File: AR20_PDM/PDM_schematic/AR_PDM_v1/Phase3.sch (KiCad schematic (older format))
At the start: 15 parts, among them Q1 BTS50025-1TAD, U1 INA233

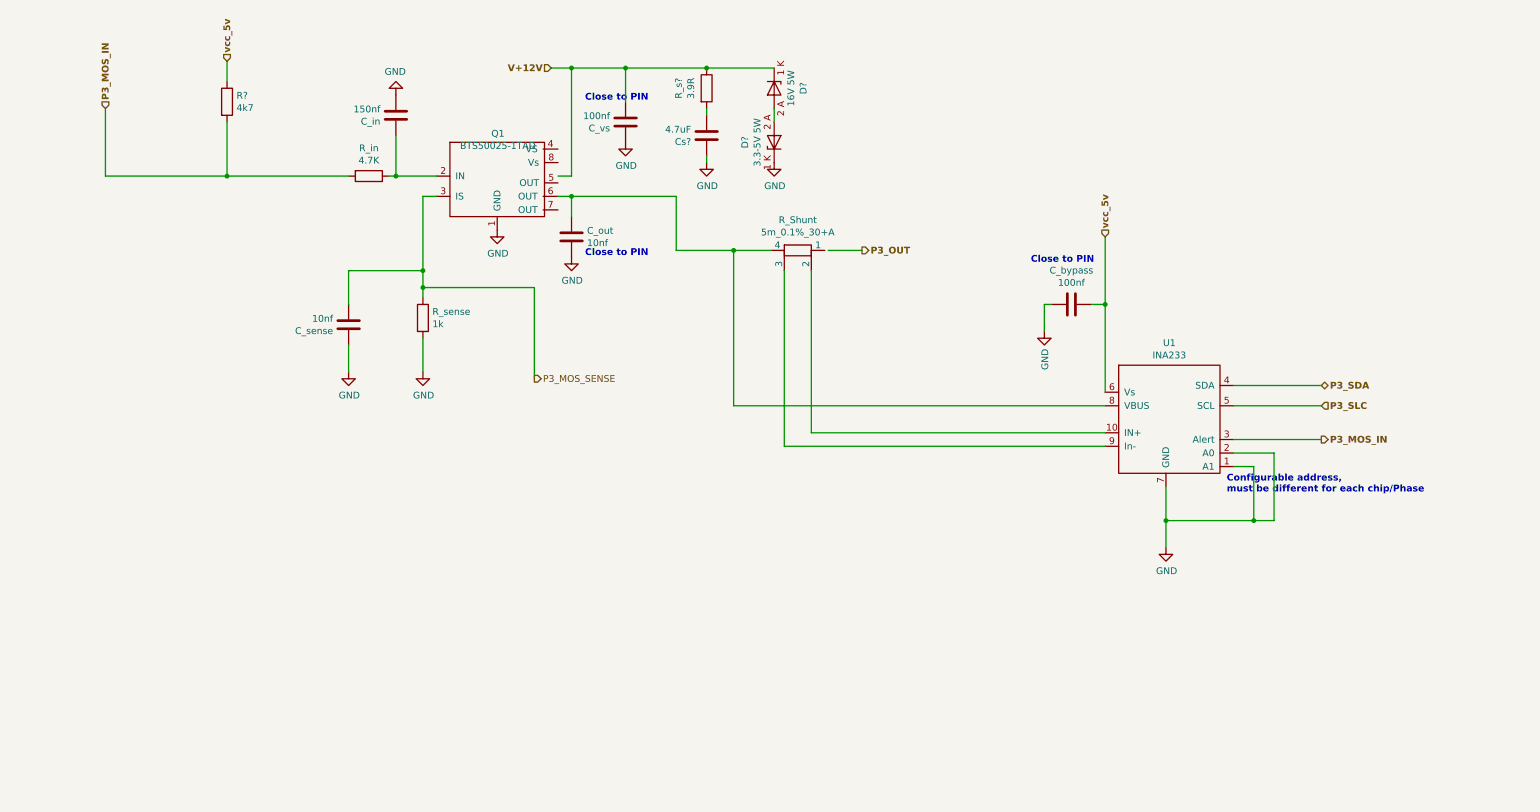
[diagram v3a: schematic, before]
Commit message: Fixed issues, controlled components, BOM, see discription
- added acm symbol
- fixed wrongly faced P-mosfets
- I/O expander now sinks led instead of source
- Bill of material mostly done
- Correct address for INA233 chips.
- Now 4 diodes serves as flyback for all mosfets
- Corrected naming scheme for compmonents (everything is not fixed yet)
- Fixed some labels
- altso some minor changes
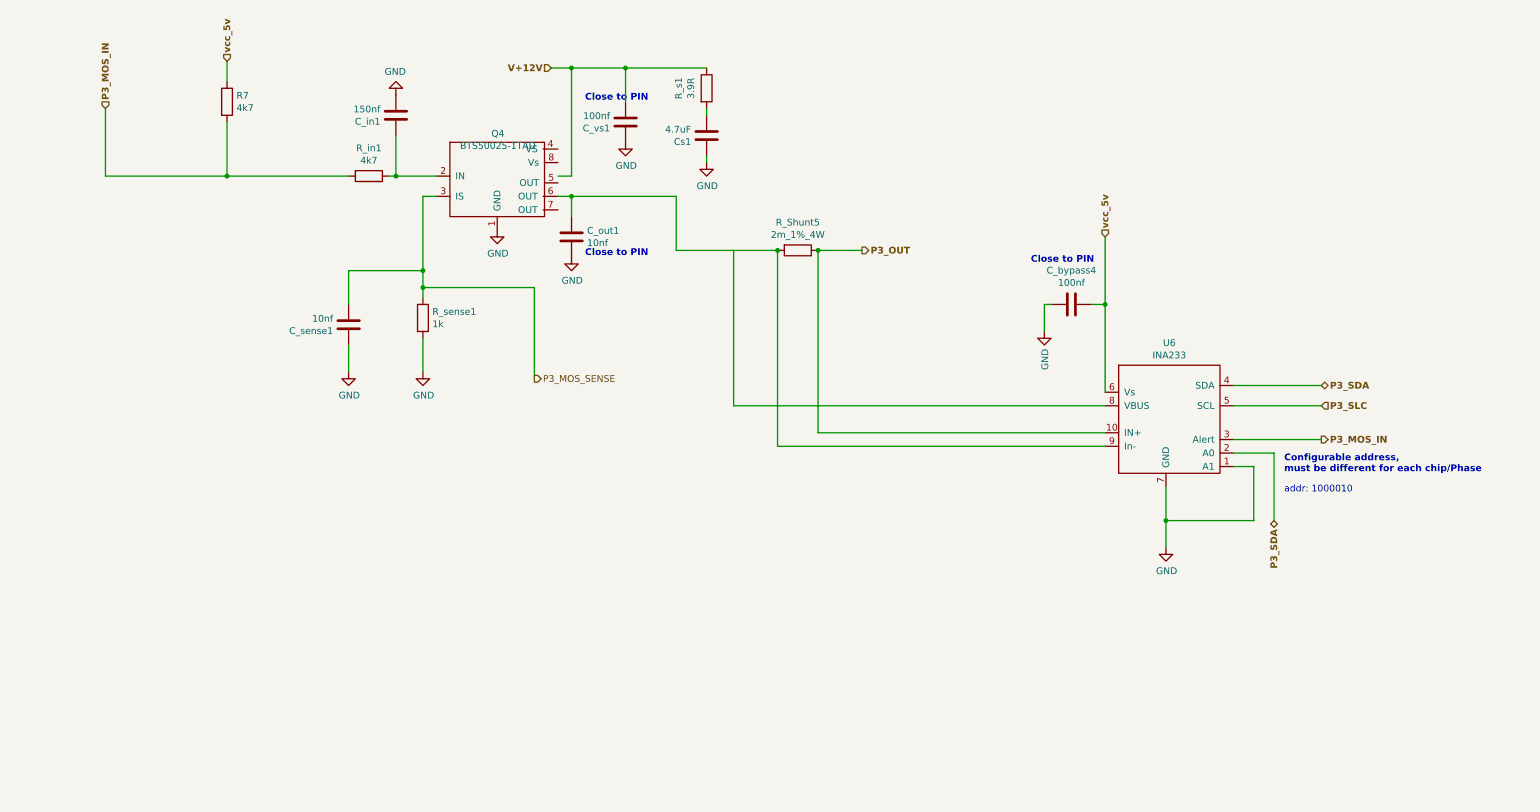
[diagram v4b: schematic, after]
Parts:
- removed C_bypass, C_vs: 100nf, symbol AR20_PDM_v1-rescue:C-Device
- removed C_in: 150nf, symbol AR20_PDM_v1-rescue:C-Device
- removed C_out, C_sense: 10nf, symbol AR20_PDM_v1-rescue:C-Device
- removed Cs?: 4.7uF, symbol AR20_PDM_v1-rescue:C-Device
- removed D?: 3.3-5V 5W, symbol AR20_PDM_v1-rescue:D_Zener-Device
- removed D?: 16V 5W, symbol AR20_PDM_v1-rescue:D_Zener-Device
- removed Q1: BTS50025-1TAD, symbol AR20_PDM_v1-rescue:BTS50025-1TAD
- removed R?: 4k7, symbol AR20_PDM_v1-rescue:R-Device
- removed R_Shunt: 5m_0.1%_30+A, symbol AR20_PDM_v1-rescue:R_Shunt-Device
- removed R_in: 4.7K, symbol AR20_PDM_v1-rescue:R-Device
- removed R_s?: 3.9R, symbol AR20_PDM_v1-rescue:R-Device
- removed R_sense: 1k, symbol AR20_PDM_v1-rescue:R-Device
- added C_bypass4, C_vs1: 100nf, Capacitor_SMD:C_0603_1608Metric, symbol AR20_PDM_v1-rescue:C-Device
- added C_in1: 150nf, Capacitor_SMD:C_0603_1608Metric, symbol AR20_PDM_v1-rescue:C-Device
- added C_out1, C_sense1: 10nf, Capacitor_SMD:C_0603_1608Metric, symbol AR20_PDM_v1-rescue:C-Device
- added Cs1: 4.7uF, Capacitor_SMD:C_1206_3216Metric, symbol AR20_PDM_v1-rescue:C-Device
- added Q4: BTS50025-1TAD, symbol AR20_PDM_v1-rescue:BTS50025-1TAD
- added R7, R_in1: 4k7, symbol AR20_PDM_v1-rescue:R-Device
- added R_Shunt5: 2m_1%_4W, symbol AR20_PDM_v1-rescue:R-Device
- added R_s1: 3.9R, symbol AR20_PDM_v1-rescue:R-Device
- added R_sense1: 1k, symbol AR20_PDM_v1-rescue:R-Device
- renumbered U1 to U6
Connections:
- wire segments 57 -> 54
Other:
- note added: "addr: 1000010"

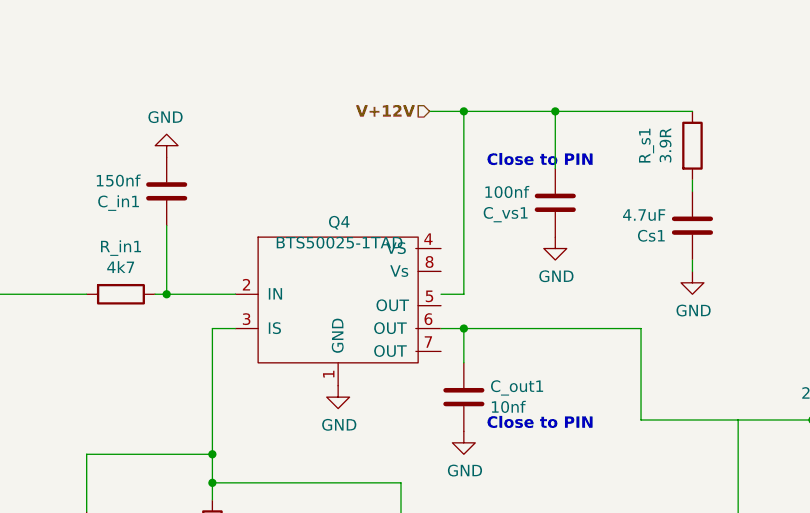
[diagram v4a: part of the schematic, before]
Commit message: PCB design, and issue fixing, work in progress
- Error fixed: Mux mosfet resistor change to ground
- Open drain output added on phase 6, for engine blipping purpose
- Most of pcb symbols and footprints are finished, including main connector
- PCB is change from 1oz to 2oz copper layer, for easier routing.
- Basic Draft of pcb is done, for now.
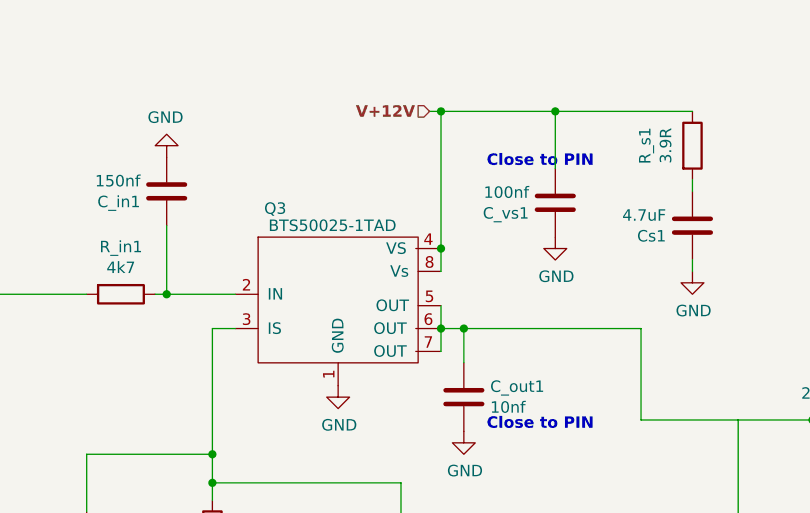
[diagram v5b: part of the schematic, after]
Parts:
- Q3: renamed from Q4; footprint (none) -> AR_PDM_v1:BTS500xx
- R7, R_in1, R_s1, R_sense1: footprint (none) -> Resistor_SMD:R_0603_1608Metric
- R_Shunt5: footprint (none) -> Resistor_SMD:R_2512_6332Metric
- U6: footprint (none) -> AR_PDM_v1:INA233
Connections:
- net V+12V: now also Q3.4 (VS), Q3.8 (Vs)
- net at C_out1.1, Q3.6 (OUT), R_Shunt5.2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: now also Q3.5 (OUT), Q3.7 (OUT)
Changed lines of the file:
@@
 F 0 "R_in1" V 3093 2400 50  0000 C CNN
 F 1 "4k7" V 3184 2400 50  0000 C CNN
-F 2 "" V 3230 2400 50  0001 C CNN
+F 2 "Resistor_SMD:R_0603_1608Metric" V 3230 2400 50  0001 C CNN
 F 3 "~" H 3300 2400 50  0001 C CNN
 	1    3300 2400
@@
 F 0 "R7" H 2320 1896 50  0000 L CNN
 F 1 "4k7" H 2320 1805 50  0000 L CNN
-F 2 "" V 2180 1850 50  0001 C CNN
+F 2 "Resistor_SMD:R_0603_1608Metric" V 2180 1850 50  0001 C CNN
 F 3 "~" H 2250 1850 50  0001 C CNN
 	1    2250 1850
@@
 AR Path="/5E0E607C/5E21B7FC" Ref="Q?"  Part="1"
 AR Path="/5E0FB5C8/5E21B7FC" Ref="Q?"  Part="1"
-AR Path="/5E0FBBBD/5E21B7FC" Ref="Q4"  Part="1"
+AR Path="/5E0FBBBD/5E21B7FC" Ref="Q3"  Part="1"
 AR Path="/5E0FC3A2/5E21B7FC" Ref="Q?"  Part="1"
 AR Path="/5E0FCFDC/5E21B7FC" Ref="Q?"  Part="1"
 AR Path="/5E0FDCCC/5E21B7FC" Ref="Q?"  Part="1"
 AR Path="/5E10174B/5E21B7FC" Ref="Q?"  Part="1"
-F 0 "Q4" H 4255 3215 50  0000 C CNN
-F 1 "BTS50025-1TAD" H 4255 3124 50  0000 C CNN
-F 2 "" H 4250 2650 50  0001 C CNN
+F 0 "Q3" H 3975 3275 50  0000 C CNN
+F 1 "BTS50025-1TAD" H 4225 3200 50  0000 C CNN
+F 2 "AR_PDM_v1:BTS500xx" H 4250 2650 50  0001 C CNN
 F 3 "" H 4250 2650 50  0001 C CNN
 	1    4250 2650
@@
 F 0 "U6" H 9225 4465 50  0000 C CNN
 F 1 "INA233" H 9225 4374 50  0000 C CNN
-F 2 "" H 9200 4050 50  0001 C CNN
+F 2 "AR_PDM_v1:INA233" H 9200 4050 50  0001 C CNN
 F 3 "" H 9200 4050 50  0001 C CNN
 	1    9200 4050
@@
 Wire Wire Line
 	3700 3100 3700 3225
-Wire Wire Line
-	4700 2400 4800 2400
-Wire Wire Line
-	4800 2400 4800 1600
-Wire Wire Line
-	4800 1600 4650 1600
 Text HLabel 2250 1550 1    50   Input ~ 10
 vcc_5v
@@
 F 0 "R_s1" V 5593 1750 50  0000 C CNN
 F 1 "3.9R" V 5684 1750 50  0000 C CNN
-F 2 "" V 5730 1750 50  0001 C CNN
+F 2 "Resistor_SMD:R_0603_1608Metric" V 5730 1750 50  0001 C CNN
 F 3 "~" H 5800 1750 50  0001 C CNN
 	1    5800 1750
@@
 Wire Wire Line
 	5200 1600 5800 1600
-Wire Wire Line
-	4800 1600 5200 1600
-Connection ~ 4800 1600
 Connection ~ 5200 1600
 Text HLabel 1350 1900 1    50   Input ~ 10
@@
 F 0 "R_sense1" H 3770 3496 50  0000 L CNN
 F 1 "1k" H 3770 3405 50  0000 L CNN
-F 2 "" V 3630 3450 50  0001 C CNN
+F 2 "Resistor_SMD:R_0603_1608Metric" V 3630 3450 50  0001 C CNN
 F 3 "~" H 3700 3450 50  0001 C CNN
 	1    3700 3450
@@
 F 0 "R_Shunt5" V 6268 2950 50  0000 C CNN
 F 1 "2m_1%_4W" V 6359 2950 50  0000 C CNN
-F 2 "" V 6405 2950 50  0001 C CNN
+F 2 "Resistor_SMD:R_2512_6332Metric" V 6405 2950 50  0001 C CNN
 F 3 "~" H 6475 2950 50  0001 C CNN
 	1    6475 2950
@@
 Text HLabel 10000 4950 3    50   BiDi ~ 10
 P3_SDA
+Wire Wire Line
+	4650 1600 4700 1600
+Wire Wire Line
+	4700 2300 4700 2200
+Wire Wire Line
+	4700 2200 4700 1600
+Connection ~ 4700 2200
+Connection ~ 4700 1600
+Wire Wire Line
+	4700 1600 5200 1600
+Wire Wire Line
+	4700 2550 4700 2650
+Connection ~ 4700 2550
+Wire Wire Line
+	4700 2550 4700 2450
 $EndSCHEMATC

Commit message: PCB Design, Work in progress
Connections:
- net P3_Shunt: now reaches C_out1.1, Q3.5 (OUT), Q3.6 (OUT), Q3.7 (OUT), R_Shunt5.2, U6.8 (VBUS), U6.9 (In-)
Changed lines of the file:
@@
 $Descr A4 11693 8268
 encoding utf-8
-Sheet 5 13
+Sheet 4 13
 Title ""
 Date ""
@@
 P3_MOS_SENSE
 Wire Wire Line
-	6000 4100 6000 2950
-Wire Wire Line
 	5575 2950 6000 2950
 Text HLabel 6950 2950 2    50   Output ~ 10
@@
 Wire Wire Line
 	4700 2550 4700 2450
+Wire Wire Line
+	6000 4100 6000 2950
+Wire Wire Line
+	6000 2950 6000 2825
+Text HLabel 6000 2825 1    50   Input ~ 0
+P3_Shunt
+Connection ~ 6000 2950
 $EndSCHEMATC

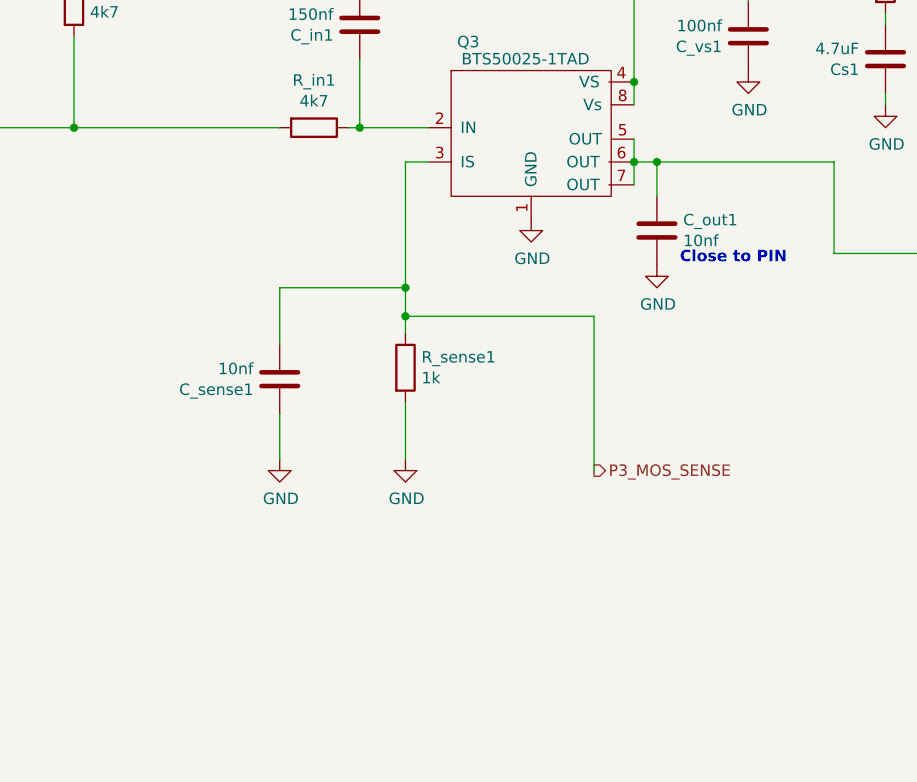
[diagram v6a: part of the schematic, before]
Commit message: PCB Design,  minor schematics changes, work in progress, see description
- Removed mos sense caps and resistors accept one, 
since only one measurement can be done, at a time.
- added mos sens protection resistors on each line, to protect mux mosfets and micro controller. 
- Routing plan mostly finalized, some of the traces are just proof of concept.
those needs to be routed nicely.
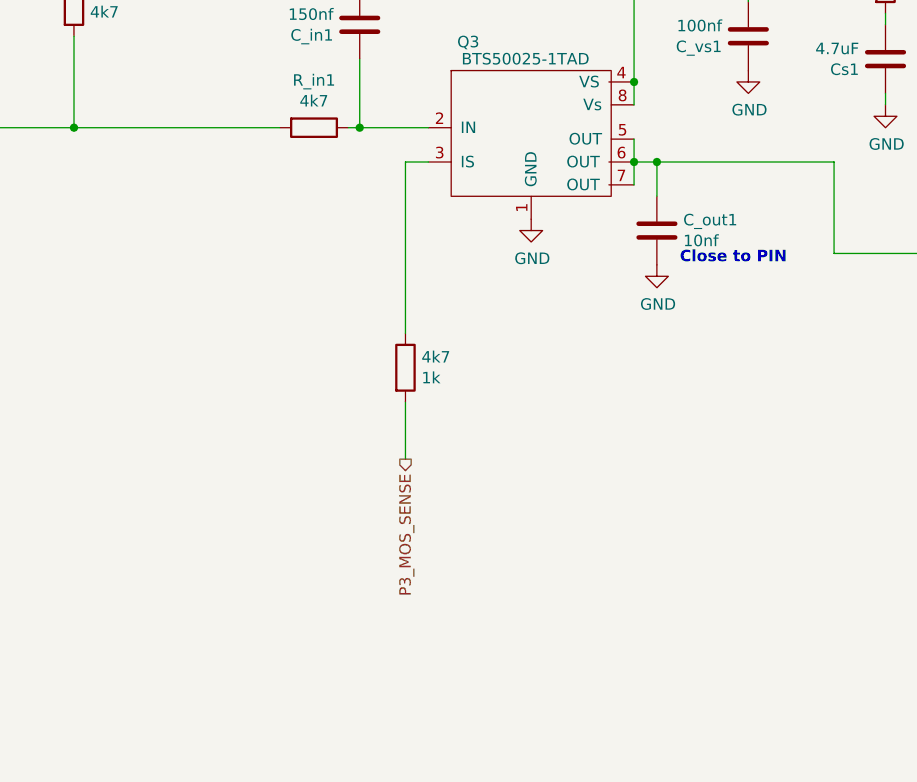
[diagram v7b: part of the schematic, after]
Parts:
- removed C_sense1: 10nf, Capacitor_SMD:C_0603_1608Metric, symbol AR20_PDM_v1-rescue:C-Device
- renumbered R_sense1 to 4k7
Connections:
- net GND: no longer 4k7.2
- net P3_MOS_SENSE: now also 4k7.2; no longer 4k7.1, Q3.3 (IS)
- new net: 4k7.1, Q3.3 (IS)
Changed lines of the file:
@@
-$EndComp
-$Comp
-L AR20_PDM_v1-rescue:GND-power #PWR?
-U 1 1 5E21B81E
-P 3700 3850
-AR Path="/5DA89415/5E21B81E" Ref="#PWR?"  Part="1"
-AR Path="/5DEB10A1/5E21B81E" Ref="#PWR?"  Part="1"
-AR Path="/5DEB20EA/5E21B81E" Ref="#PWR?"  Part="1"
-AR Path="/5E0E4725/5E21B81E" Ref="#PWR?"  Part="1"
-AR Path="/5E0E4A93/5E21B81E" Ref="#PWR?"  Part="1"
-AR Path="/5E0E4EB5/5E21B81E" Ref="#PWR?"  Part="1"
-AR Path="/5E0E5304/5E21B81E" Ref="#PWR?"  Part="1"
-AR Path="/5E0E594B/5E21B81E" Ref="#PWR?"  Part="1"
-AR Path="/5E0E607C/5E21B81E" Ref="#PWR?"  Part="1"
-AR Path="/5E0FB5C8/5E21B81E" Ref="#PWR?"  Part="1"
-AR Path="/5E0FBBBD/5E21B81E" Ref="#PWR037"  Part="1"
-AR Path="/5E0FC3A2/5E21B81E" Ref="#PWR?"  Part="1"
-AR Path="/5E0FCFDC/5E21B81E" Ref="#PWR?"  Part="1"
-AR Path="/5E0FDCCC/5E21B81E" Ref="#PWR?"  Part="1"
-AR Path="/5E10174B/5E21B81E" Ref="#PWR?"  Part="1"
-F 0 "#PWR037" H 3700 3600 50  0001 C CNN
-F 1 "GND" H 3705 3677 50  0000 C CNN
-F 2 "" H 3700 3850 50  0001 C CNN
-F 3 "" H 3700 3850 50  0001 C CNN
-	1    3700 3850
-	1    0    0    -1
 $EndComp
 $Comp
@@
 $EndComp
 Wire Wire Line
-	3700 2550 3700 3100
-Wire Wire Line
 	3700 2550 3800 2550
 Wire Wire Line
@@
 Wire Wire Line
 	9700 4450 10000 4450
-$Comp
-L AR20_PDM_v1-rescue:GND-power #PWR?
-U 1 1 5DAAC27D
-P 3150 3850
-AR Path="/5DA89415/5DAAC27D" Ref="#PWR?"  Part="1"
-AR Path="/5DEB10A1/5DAAC27D" Ref="#PWR?"  Part="1"
-AR Path="/5DEB20EA/5DAAC27D" Ref="#PWR?"  Part="1"
-AR Path="/5E0E4725/5DAAC27D" Ref="#PWR?"  Part="1"
-AR Path="/5E0E4A93/5DAAC27D" Ref="#PWR?"  Part="1"
-AR Path="/5E0E4EB5/5DAAC27D" Ref="#PWR?"  Part="1"
-AR Path="/5E0E5304/5DAAC27D" Ref="#PWR?"  Part="1"
-AR Path="/5E0E594B/5DAAC27D" Ref="#PWR?"  Part="1"
-AR Path="/5E0E607C/5DAAC27D" Ref="#PWR?"  Part="1"
-AR Path="/5E0FB5C8/5DAAC27D" Ref="#PWR?"  Part="1"
-AR Path="/5E0FBBBD/5DAAC27D" Ref="#PWR035"  Part="1"
-AR Path="/5E0FC3A2/5DAAC27D" Ref="#PWR?"  Part="1"
-AR Path="/5E0FCFDC/5DAAC27D" Ref="#PWR?"  Part="1"
-AR Path="/5E0FDCCC/5DAAC27D" Ref="#PWR?"  Part="1"
-AR Path="/5E10174B/5DAAC27D" Ref="#PWR?"  Part="1"
-F 0 "#PWR035" H 3150 3600 50  0001 C CNN
-F 1 "GND" H 3155 3677 50  0000 C CNN
-F 2 "" H 3150 3850 50  0001 C CNN
-F 3 "" H 3150 3850 50  0001 C CNN
-	1    3150 3850
-	1    0    0    -1
-$EndComp
-$Comp
-L AR20_PDM_v1-rescue:C-Device C_sense?
-U 1 1 5E21B84E
-P 3150 3500
-AR Path="/5DA89415/5E21B84E" Ref="C_sense?"  Part="1"
-AR Path="/5DEB10A1/5E21B84E" Ref="C_sense?"  Part="1"
-AR Path="/5DEB20EA/5E21B84E" Ref="C_sense?"  Part="1"
-AR Path="/5E0E4725/5E21B84E" Ref="C_sense?"  Part="1"
-AR Path="/5E0E4A93/5E21B84E" Ref="C_sense?"  Part="1"
-AR Path="/5E0E4EB5/5E21B84E" Ref="C_sense?"  Part="1"
-AR Path="/5E0E5304/5E21B84E" Ref="C_sense?"  Part="1"
-AR Path="/5E0E594B/5E21B84E" Ref="C_sense?"  Part="1"
-AR Path="/5E0E607C/5E21B84E" Ref="C_sense?"  Part="1"
-AR Path="/5E0FB5C8/5E21B84E" Ref="C_sense?"  Part="1"
-AR Path="/5E0FBBBD/5E21B84E" Ref="C_sense1"  Part="1"
-AR Path="/5E0FC3A2/5E21B84E" Ref="C_sense?"  Part="1"
-AR Path="/5E0FCFDC/5E21B84E" Ref="C_sense?"  Part="1"
-AR Path="/5E0FDCCC/5E21B84E" Ref="C_sense?"  Part="1"
-AR Path="/5E10174B/5E21B84E" Ref="C_sense?"  Part="1"
-F 0 "C_sense1" H 3265 3546 50  0000 L CNN
-F 1 "10nf" H 3265 3455 50  0000 L CNN
-F 2 "Capacitor_SMD:C_0603_1608Metric" H 3188 3350 50  0001 C CNN
-F 3 "~" H 3150 3500 50  0001 C CNN
-	1    3150 3500
-	-1   0    0    1
-$EndComp
 Wire Wire Line
 	3450 2400 3500 2400
@@
 Text Notes 8200 3050 0    50   ~ 10
 Close to PIN
-Wire Wire Line
-	3150 3100 3150 3350
-Wire Wire Line
-	3150 3650 3150 3850
-Wire Wire Line
-	3150 3100 3700 3100
-Connection ~ 3700 3100
-Wire Wire Line
-	3700 3100 3700 3225
 Text HLabel 2250 1550 1    50   Input ~ 10
 vcc_5v
@@
 AR Path="/5E0E607C/5E21B876" Ref="R_sense?"  Part="1"
 AR Path="/5E0FB5C8/5E21B876" Ref="R_sense?"  Part="1"
-AR Path="/5E0FBBBD/5E21B876" Ref="R_sense1"  Part="1"
+AR Path="/5E0FBBBD/5E21B876" Ref="4k7"  Part="1"
 AR Path="/5E0FC3A2/5E21B876" Ref="R_sense?"  Part="1"
 AR Path="/5E0FCFDC/5E21B876" Ref="R_sense?"  Part="1"
 AR Path="/5E0FDCCC/5E21B876" Ref="R_sense?"  Part="1"
 AR Path="/5E10174B/5E21B876" Ref="R_sense?"  Part="1"
-F 0 "R_sense1" H 3770 3496 50  0000 L CNN
+F 0 "4k7" H 3770 3496 50  0000 L CNN
 F 1 "1k" H 3770 3405 50  0000 L CNN
 F 2 "Resistor_SMD:R_0603_1608Metric" V 3630 3450 50  0001 C CNN
@@
 Wire Wire Line
 	6625 4300 8750 4300
-Wire Wire Line
-	3700 3225 4525 3225
-Wire Wire Line
-	4525 3225 4525 3900
-Connection ~ 3700 3225
-Wire Wire Line
-	3700 3225 3700 3300
-Text HLabel 4525 3900 2    50   Output ~ 0
+Text HLabel 3700 3850 3    50   Output ~ 0
 P3_MOS_SENSE
 Wire Wire Line
@@
 P3_Shunt
 Connection ~ 6000 2950
+Wire Wire Line
+	3700 2550 3700 3300
 $EndSCHEMATC
